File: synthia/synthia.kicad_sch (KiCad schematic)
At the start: 116 parts, among them Q1 IRF9540N, Q2 L78M05CV

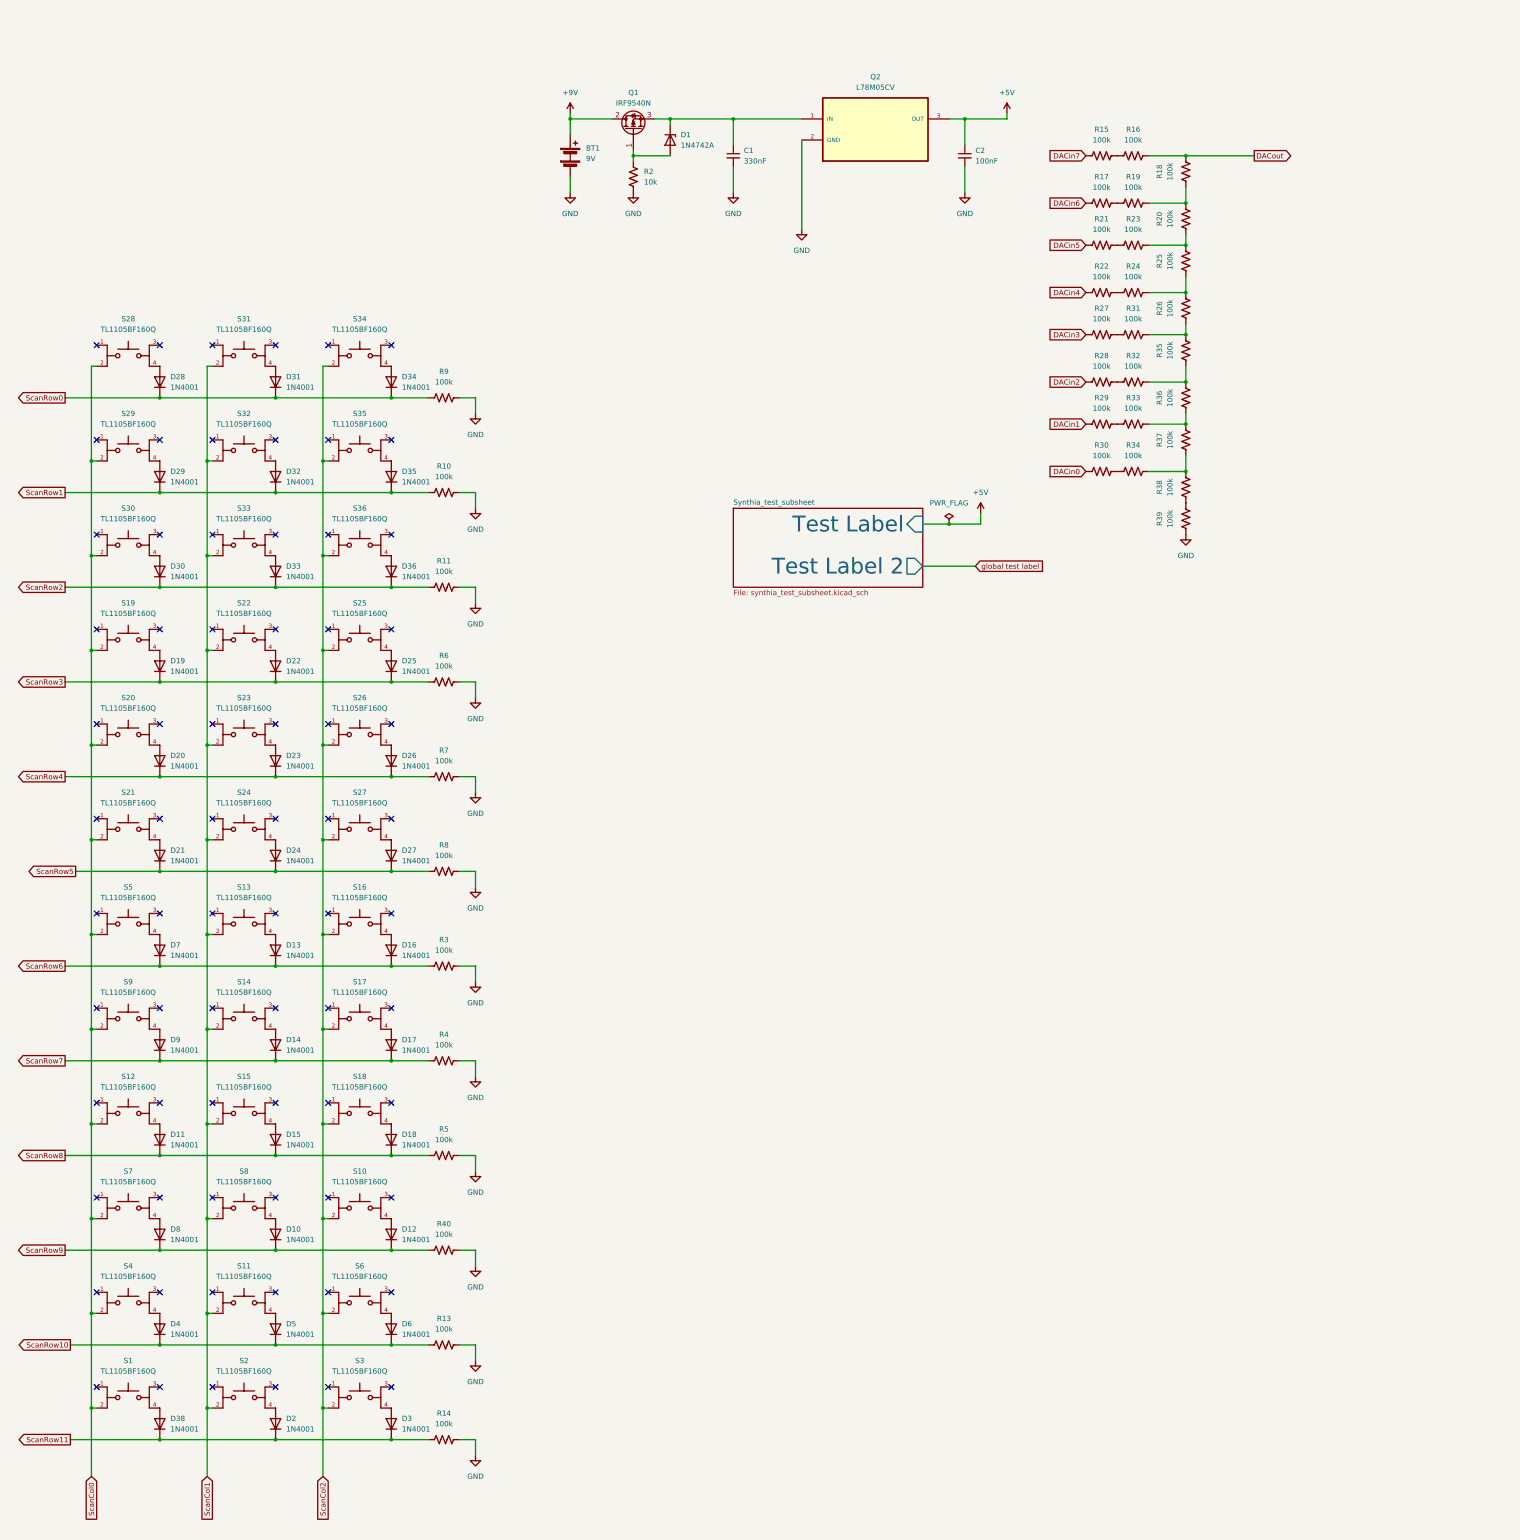
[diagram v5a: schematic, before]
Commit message: Embedded DAC and Button Matrix into IC style subsheets (Not Documented
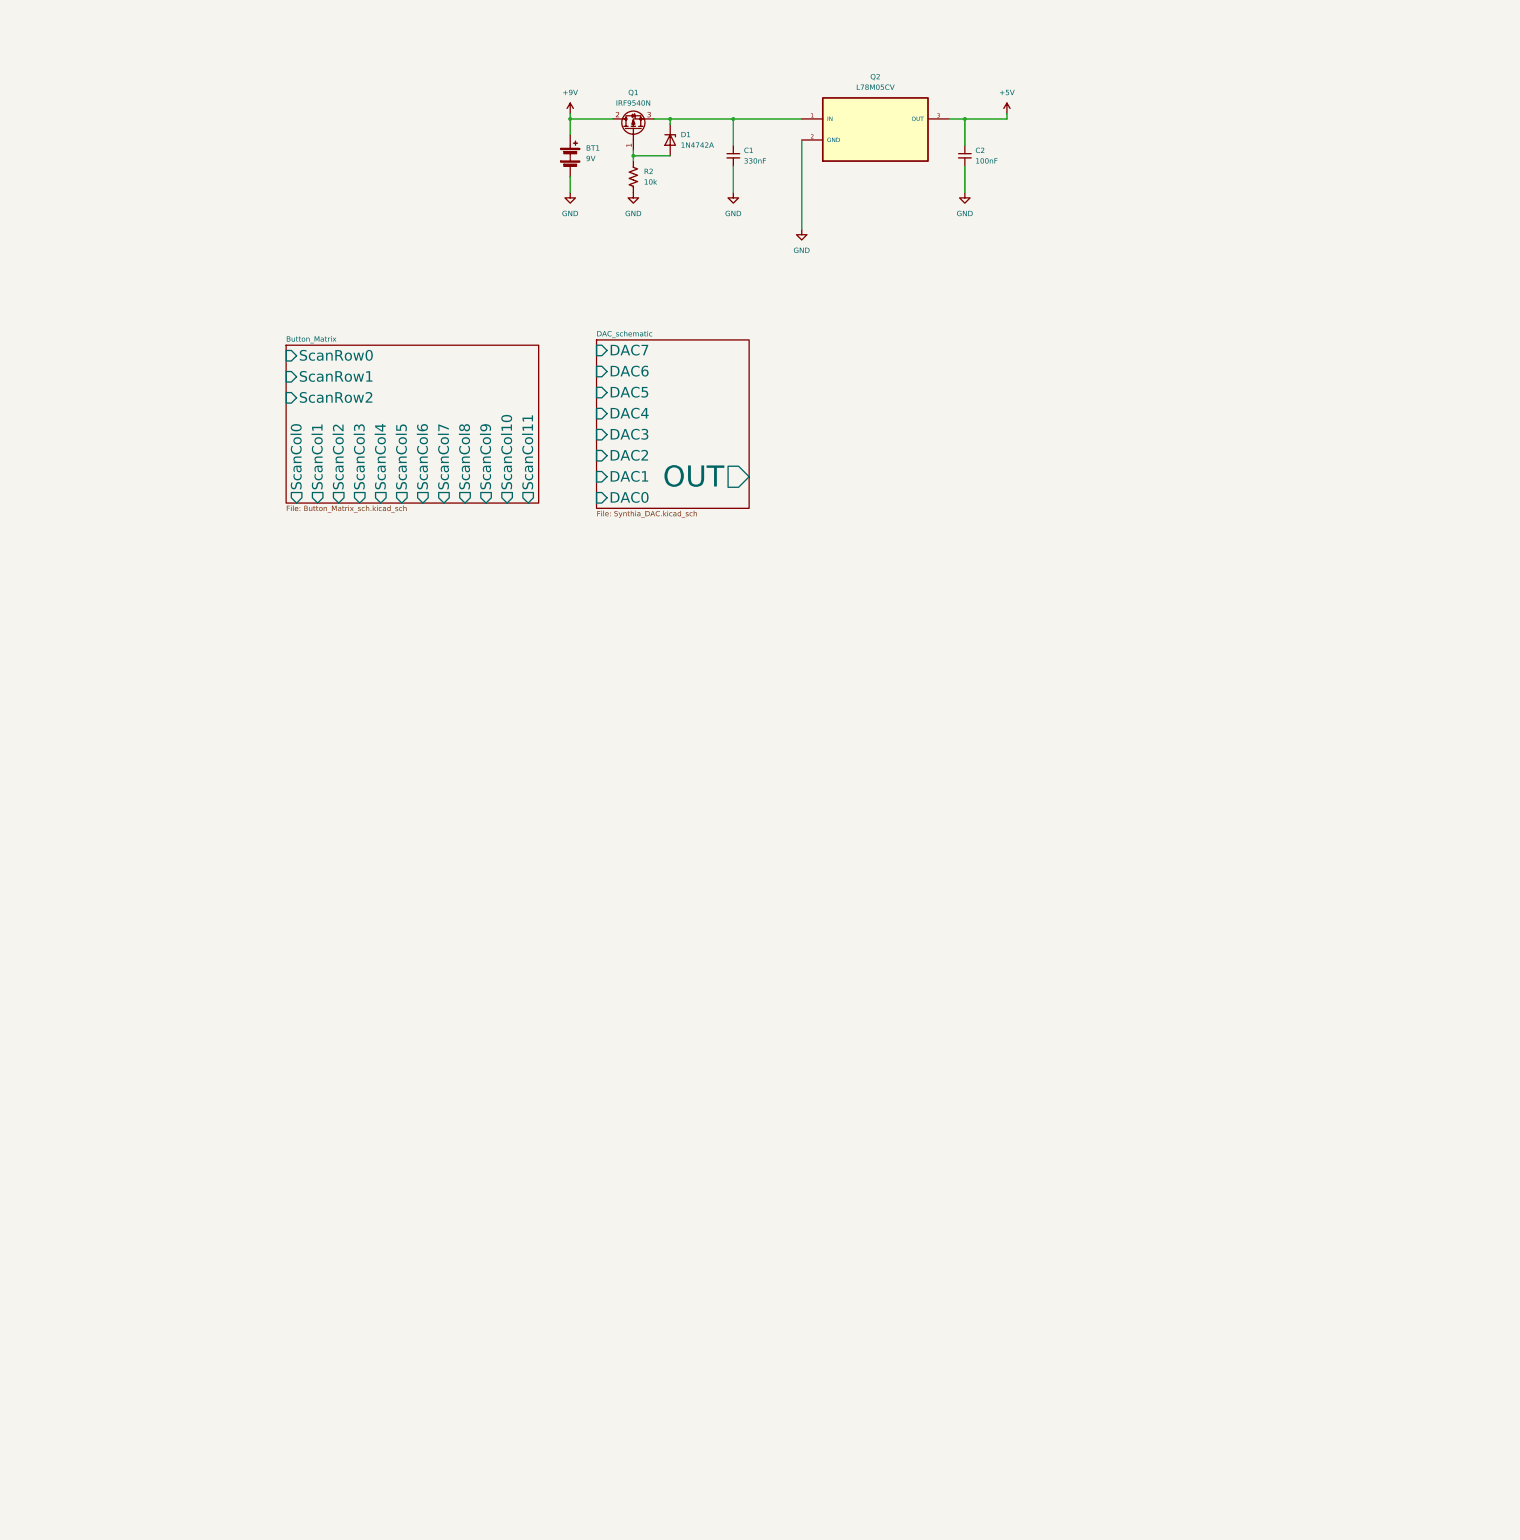
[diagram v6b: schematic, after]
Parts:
- removed D10, D11, D12, D13, D14, D15, D16, D17, D18, D19, D2, D20, D21, D22, D23, D24, D25, D26, D27, D28, D29, D3, D30, D31, D32, D33, D34, D35, D36, D38, D4, D5, D6, D7, D8, D9: 1N4001, Diode_THT:D_DO-41_SOD81_P10.16mm_Horizontal, symbol Diode:1N4001
- removed R10, R11, R13, R14, R15, R16, R17, R18, R19, R20, R21, R22, R23, R24, R25, R26, R27, R28, R29, R3, R30, R31, R32, R33, R34, R35, R36, R37, R38, R39, R4, R40, R5, R6, R7, R8, R9: 100k, symbol Device:R_US
- removed S1, S10, S11, S12, S13, S14, S15, S16, S17, S18, S19, S2, S20, S21, S22, S23, S24, S25, S26, S27, S28, S29, S3, S30, S31, S32, S33, S34, S35, S36, S4, S5, S6, S7, S8, S9: TL1105BF160Q, TL1105BF160Q:SW_TL1105BF160Q, symbol Synthia_Button_Symbol:TL1105BF160Q
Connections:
- no-connect marks 72 -> 0
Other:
- removed sheet Synthia_test_subsheet
- added sheet Button_Matrix (Button_Matrix_sch.kicad_sch)
- added sheet DAC_schematic (Synthia_DAC.kicad_sch)

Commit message: Started on the PCB, button matrix is active
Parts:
- Q2: footprint L78M05CV:TO254P450X1020X1935-3P -> Synthia_footprint_library:TO254P450X1020X1935-3P
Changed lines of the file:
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@@
 			)
 		)
-		(property "Footprint" "L78M05CV:TO254P450X1020X1935-3P"
+		(property "Footprint" "Synthia_footprint_library:TO254P450X1020X1935-3P"
 			(at 233.68 41.91 0)
 			(effects

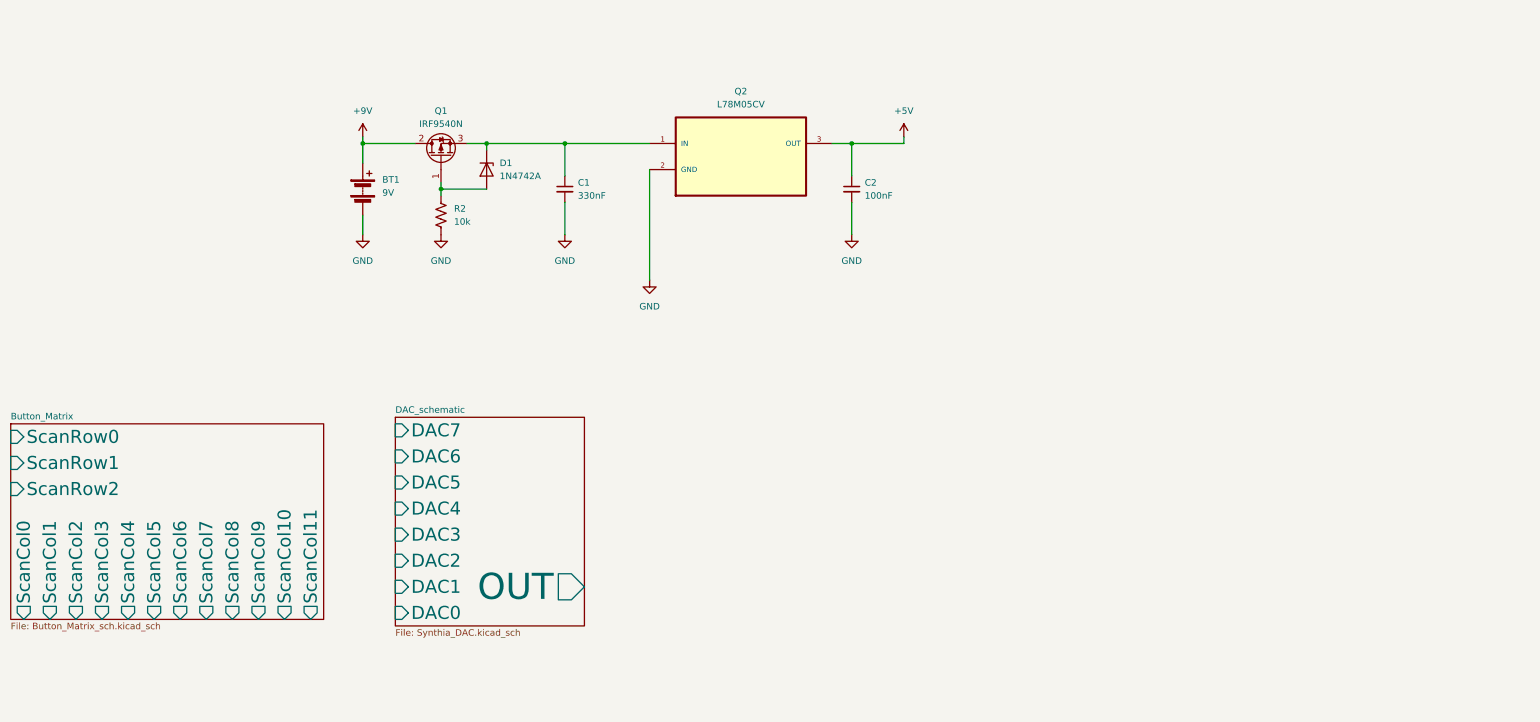
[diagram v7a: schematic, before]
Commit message: Output circuit has been made into a schematic
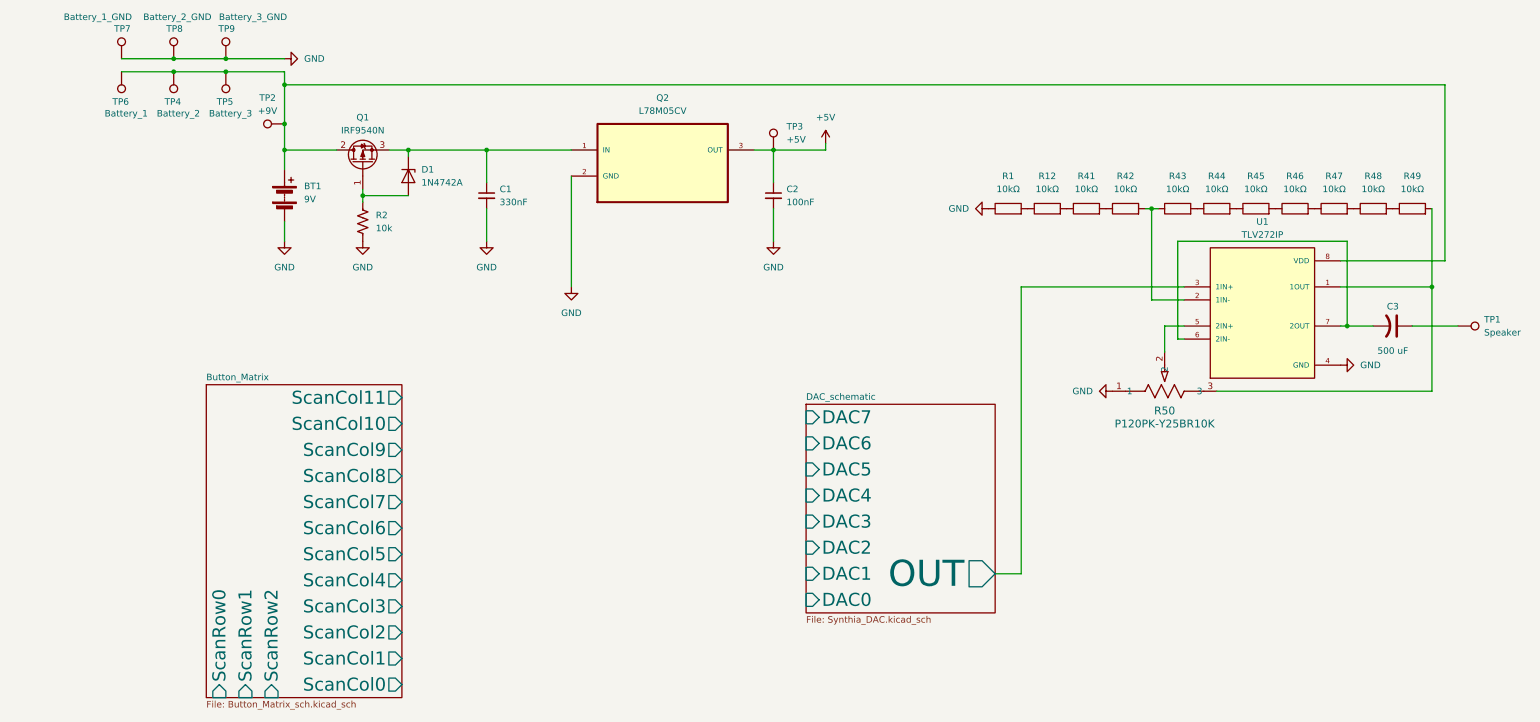
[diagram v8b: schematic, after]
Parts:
- added C3: 500 uF, symbol Device:C_US
- added R1, R12, R41, R42, R43, R44, R45, R46, R47, R48, R49: 10kΩ, symbol Device:R
- added R50: P120PK-Y25BR10K, POT_P120PK-x25_TTE, symbol Synthia_Symbol_Library:P120PK-Y25BR10K
- added TP1: Speaker, TestPoint:TestPoint_Plated_Hole_D2.0mm, symbol Connector:TestPoint
- added TP2: +9V, TestPoint:TestPoint_Pad_2.0x2.0mm, symbol Connector:TestPoint
- added TP3: +5V, TestPoint:TestPoint_Pad_2.0x2.0mm, symbol Connector:TestPoint
- added TP4: Battery_2, TestPoint:TestPoint_Plated_Hole_D2.0mm, symbol Connector:TestPoint
- added TP5: Battery_3, TestPoint:TestPoint_Plated_Hole_D2.0mm, symbol Connector:TestPoint
- added TP6: Battery_1, TestPoint:TestPoint_Plated_Hole_D2.0mm, symbol Connector:TestPoint
- added TP7: Battery_1_GND, TestPoint:TestPoint_Plated_Hole_D2.0mm, symbol Connector:TestPoint
- added TP8: Battery_2_GND, TestPoint:TestPoint_Plated_Hole_D2.0mm, symbol Connector:TestPoint
- added TP9: Battery_3_GND, TestPoint:TestPoint_Plated_Hole_D2.0mm, symbol Connector:TestPoint
- added U1: TLV272IP, Synthia_footprint_library:POT_P120PK-x25_TTE, symbol Synthia_Symbol_Library:TLV272IP
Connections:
- net +5V: now also TP3.1
- net DAC_schematic/OUT: now also U1.3 (1IN+)
- net GND: now also R1.1, R50.1, TP7.1, TP8.1, TP9.1, U1.4 (GND)
- net +9V: no longer names the net of BT1.1 (+), Q1.2 (D)
- net +9V: now also TP2.1, TP4.1, TP5.1, TP6.1, U1.8 (VDD)
- new net: R50.2, U1.5 (2IN+)
- new net: R49.2, R50.3, U1.1 (1OUT)
- new net: R48.2, R49.1
- new net: R43.2, R44.1
- new net: R44.2, R45.1
- new net: R45.2, R46.1
- new net: R46.2, R47.1
- new net: R1.2, R12.1
- new net: R12.2, R41.1
- new net: R41.2, R42.1
- new net: R42.2, R43.1, U1.2 (1IN-)
- new net: C3.2, U1.6 (2IN-), U1.7 (2OUT)
- new net: C3.1, TP1.1
- new net: R47.2, R48.1
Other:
- moved on the sheet: BT1, C1, C2, D1, Q1, Q2, R2
